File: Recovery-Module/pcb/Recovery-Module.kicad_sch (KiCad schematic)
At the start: 22 parts, among them J1 Conn_02x10_Odd_Even, SW1 SW_DIP_x03, U1 W25Q128JVS, U2 MCP130-xxxxTT, U3 STM32H503RBTx

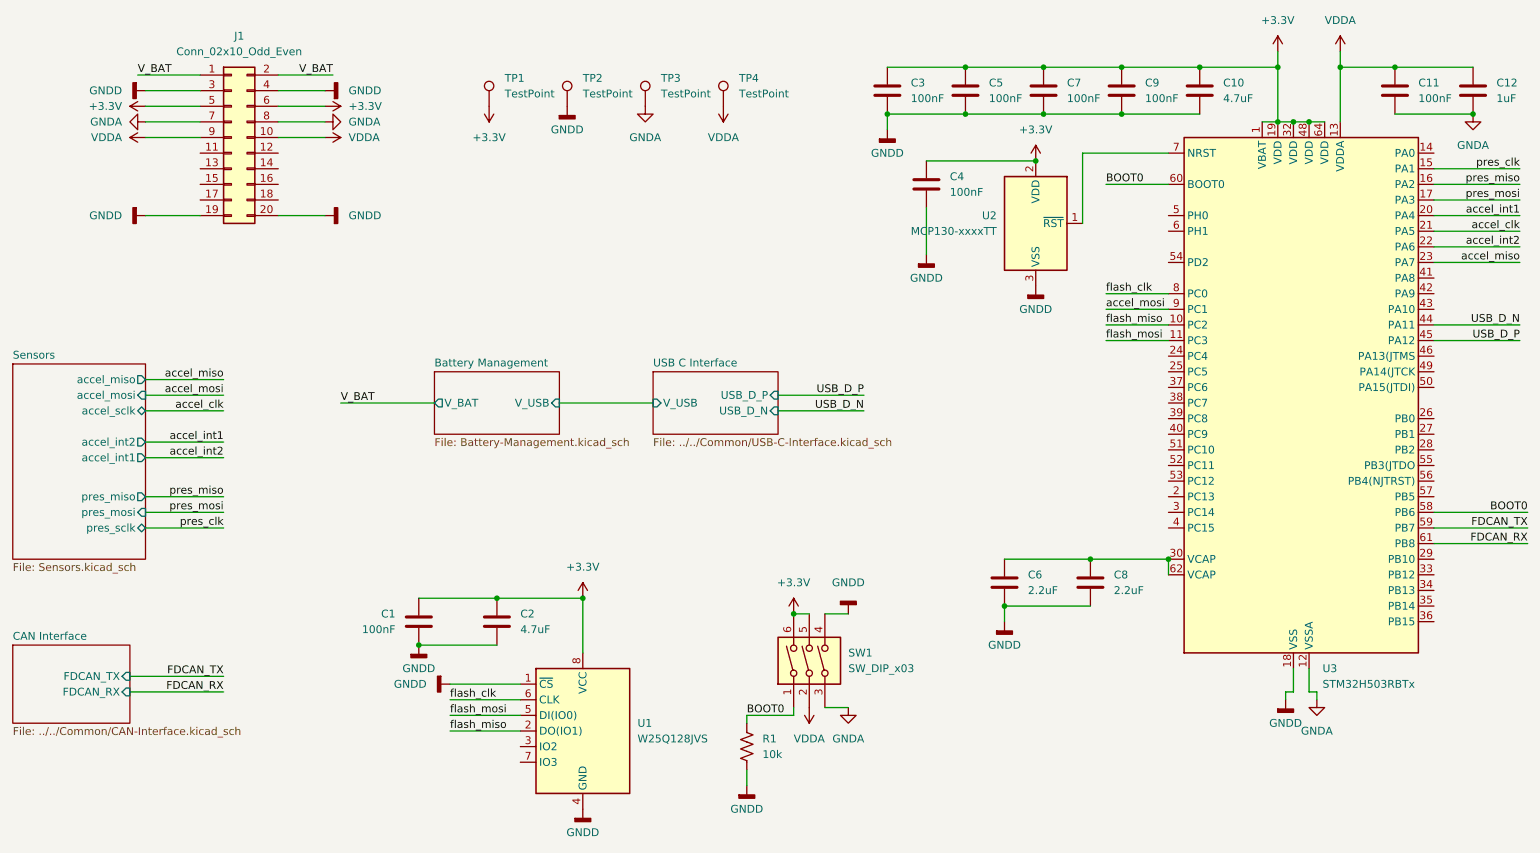
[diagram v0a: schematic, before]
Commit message: Updated Schematic
USBC, Sensor, MCU
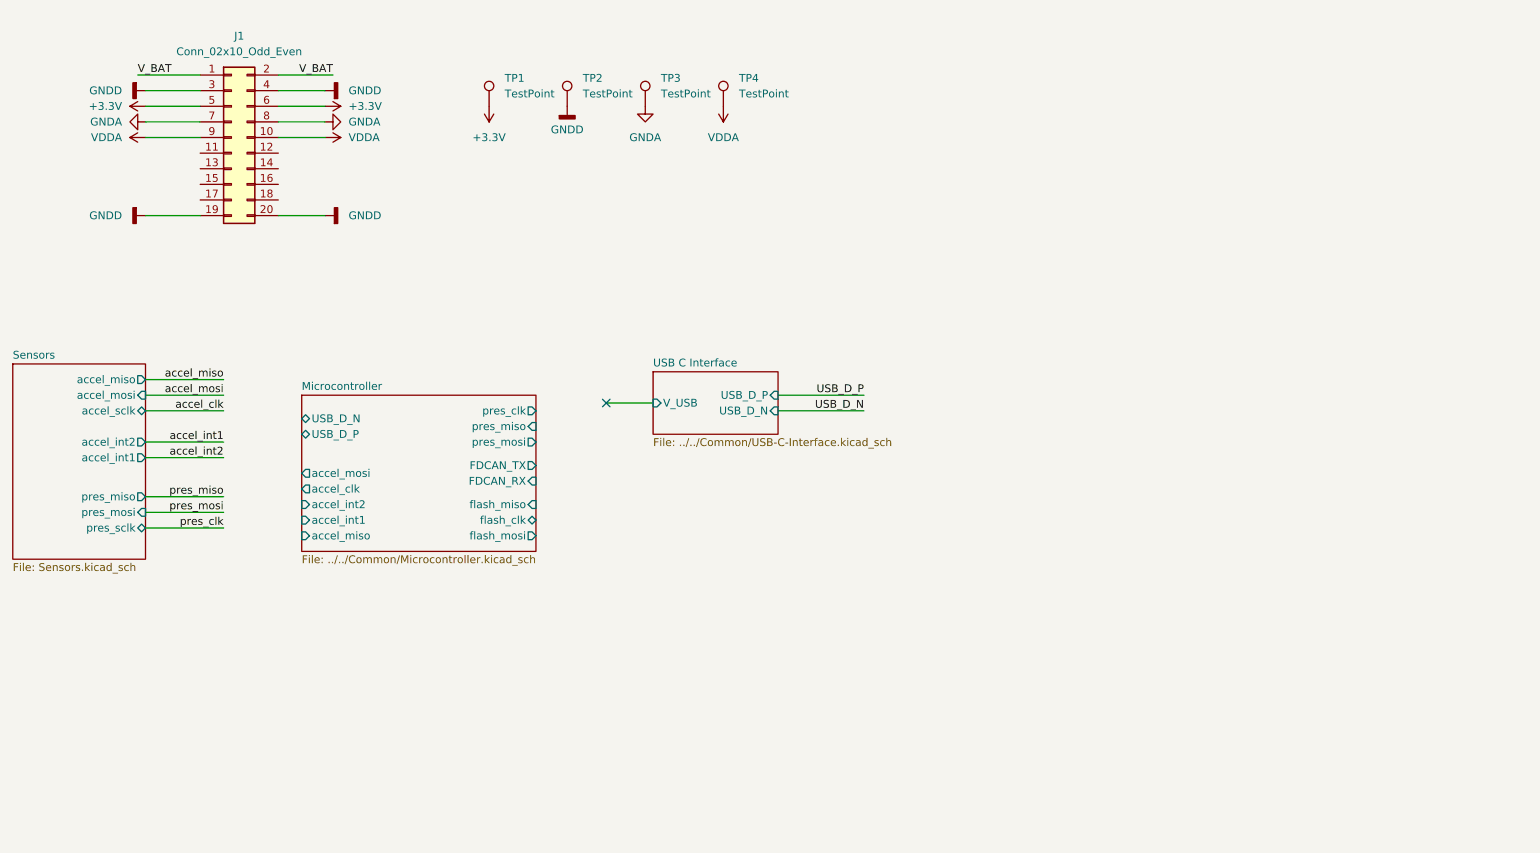
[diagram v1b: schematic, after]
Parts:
- removed C1, C11, C3, C4, C5, C7, C9: 100nF, Capacitor_SMD:C_0603_1608Metric_Pad1.08x0.95mm_HandSolder, symbol Device:C
- removed C10, C2: 4.7uF, Capacitor_SMD:C_0603_1608Metric_Pad1.08x0.95mm_HandSolder, symbol Device:C
- removed C12: 1uF, Capacitor_SMD:C_0603_1608Metric_Pad1.08x0.95mm_HandSolder, symbol Device:C
- removed C6, C8: 2.2uF, Capacitor_SMD:C_0603_1608Metric_Pad1.08x0.95mm_HandSolder, symbol Device:C
- removed R1: 10k, Resistor_SMD:R_0603_1608Metric_Pad0.98x0.95mm_HandSolder, symbol Device:R_US
- removed SW1: SW_DIP_x03, Button_Switch_THT:SW_DIP_SPSTx03_Slide_9.78x9.8mm_W7.62mm_P2.54mm, symbol Switch:SW_DIP_x03
- removed U1: W25Q128JVS, Package_SO:SOIC-8_5.23x5.23mm_P1.27mm, symbol Memory_Flash:W25Q128JVS
- removed U2: MCP130-xxxxTT, Package_TO_SOT_SMD:SOT-23, symbol Power_Supervisor:MCP130-xxxxTT
- removed U3: STM32H503RBTx, Package_QFP:LQFP-64_10x10mm_P0.5mm, symbol MCU_ST_STM32H5:STM32H503RBTx
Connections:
- no-connect marks 0 -> 1
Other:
- removed sheet Battery Management
- removed sheet CAN Interface
- added sheet Microcontroller (../../Common/Microcontroller.kicad_sch)

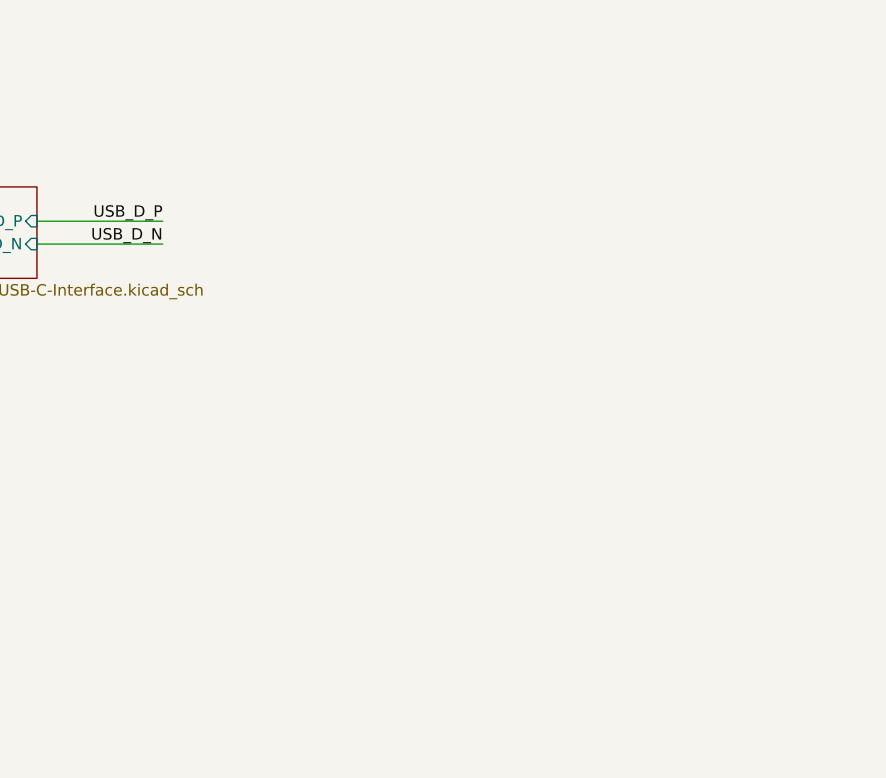
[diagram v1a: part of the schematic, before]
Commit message: Added Pyro Controller and Valve Controller to Block Diagram
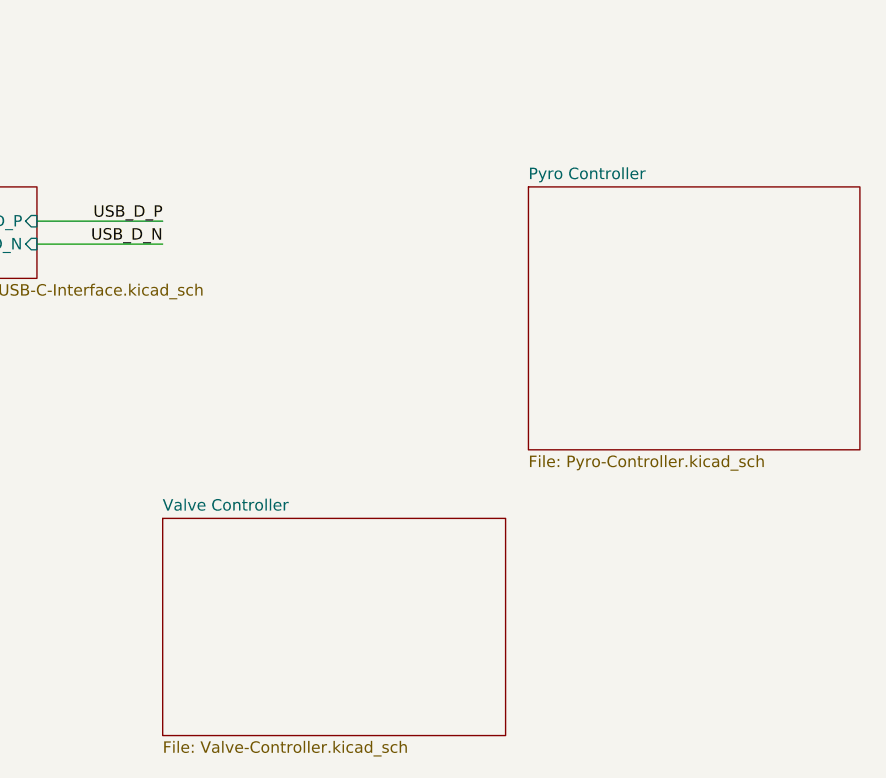
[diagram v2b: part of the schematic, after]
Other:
- added sheet Pyro Controller (Pyro-Controller.kicad_sch)
- added sheet Valve Controller (Valve-Controller.kicad_sch)
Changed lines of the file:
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@@
+	)
+	(sheet
+		(at 210.82 74.93)
+		(size 36.83 29.21)
+		(fields_autoplaced yes)
+		(stroke
+			(width 0.1524)
+			(type solid)
+		)
+		(fill
+			(color 0 0 0 0.0000)
+		)
+		(property "Sheetname" "Pyro Controller"
+			(at 210.82 74.2184 0)
+			(effects
+				(font
+					(size 1.27 1.27)
+				)
+				(justify left bottom)
+			)
+		)
+		(property "Sheetfile" "Pyro-Controller.kicad_sch"
+			(at 210.82 104.7246 0)
+			(effects
+				(font
+					(size 1.27 1.27)
+				)
+				(justify left top)
+			)
+		)
+		(instances
+			(project "Recovery-Module"
+				(path "/c41b490b-5ab6-4438-aea0-388670bb08f4"
+					(page "6")
+				)
+			)
+		)
+	)
+	(sheet
+		(at 170.18 111.76)
+		(size 38.1 24.13)
+		(fields_autoplaced yes)
+		(stroke
+			(width 0.1524)
+			(type solid)
+		)
+		(fill
+			(color 0 0 0 0.0000)
+		)
+		(property "Sheetname" "Valve Controller"
+			(at 170.18 111.0484 0)
+			(effects
+				(font
+					(size 1.27 1.27)
+				)
+				(justify left bottom)
+			)
+		)
+		(property "Sheetfile" "Valve-Controller.kicad_sch"
+			(at 170.18 136.4746 0)
+			(effects
+				(font
+					(size 1.27 1.27)
+				)
+				(justify left top)
+			)
+		)
+		(instances
+			(project "Recovery-Module"
+				(path "/c41b490b-5ab6-4438-aea0-388670bb08f4"
+					(page "5")
+				)
+			)
+		)
 	)
 	(sheet
